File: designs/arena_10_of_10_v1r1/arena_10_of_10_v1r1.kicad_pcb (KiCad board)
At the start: 6 copper layers, 248.9 x 228.6 mm, 519 parts, among them J1 Cetus RJ45 Magjack, J10 Conn_01x05, J11 Conn_01x05, J12 Conn_01x05, J13 Conn_01x05, J14 Conn_01x05, J15 Conn_01x05, J16 Conn_01x05, J17 Conn_01x05, J18 Conn_01x05, J19 Conn_01x05, J2 Conn_01x02, J20 Conn_01x05, J21 Conn_01x05, J22 Conn_01x05, J23 Conn_01x05, J24 Conn_01x05, J25 Barrel_Jack, J26 Barrel_Jack, J27 Conn_Coaxial, J28 Conn_Coaxial, J29 Conn_Coaxial, J3 Conn_Coaxial, J4 Conn_Coaxial, J5 Conn_01x05, J6 Conn_01x05, J7 Conn_01x05, J8 Conn_01x05, J9 Conn_01x05, P1 NA, P10 NA, P2 NA, P3 NA, P4 NA, P5 NA, P6 NA, P7 NA, P8 NA, P9 NA, SW1 SW_SPDT, U1 Teensy4.1, U10 74LVC2G17, U100 74LVC1G125, U101 74LVC2G17, U102 SN74HCS08, U103 SN74HCS08, U104 74LVC1G125, U105 74LVC2G17, U106 SN74HCS08, U107 SN74HCS08, U108 74LVC1G125, U109 74LVC2G17, U11 74LVC2G17, U112 74LVC1G125, U113 74LVC2G17, U116 74LVC1G125, U117 74LVC2G17, U12 74LVC2G17, U120 74LVC1G125, U121 74LVC2G17, U124 74LVC1G125, U125 74LVC2G17, U13 74LVC2G17, U14 74LVC2G17, U15 74LVC2G17, U16 74LVC2G17, U17 74LVC2G17, U18 74LVC2G17, U19 74LVC2G17, U2 SN74LV1T34DBV, U20 74LVC2G17, U21 74LVC2G17, U22 74LVC2G17, U23 74LVC2G17, U24 74LVC2G17, U25 74LVC2G17, U26 74LVC2G17, U27 74LVC2G17, U28 74LVC2G17, U29 74LVC2G17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

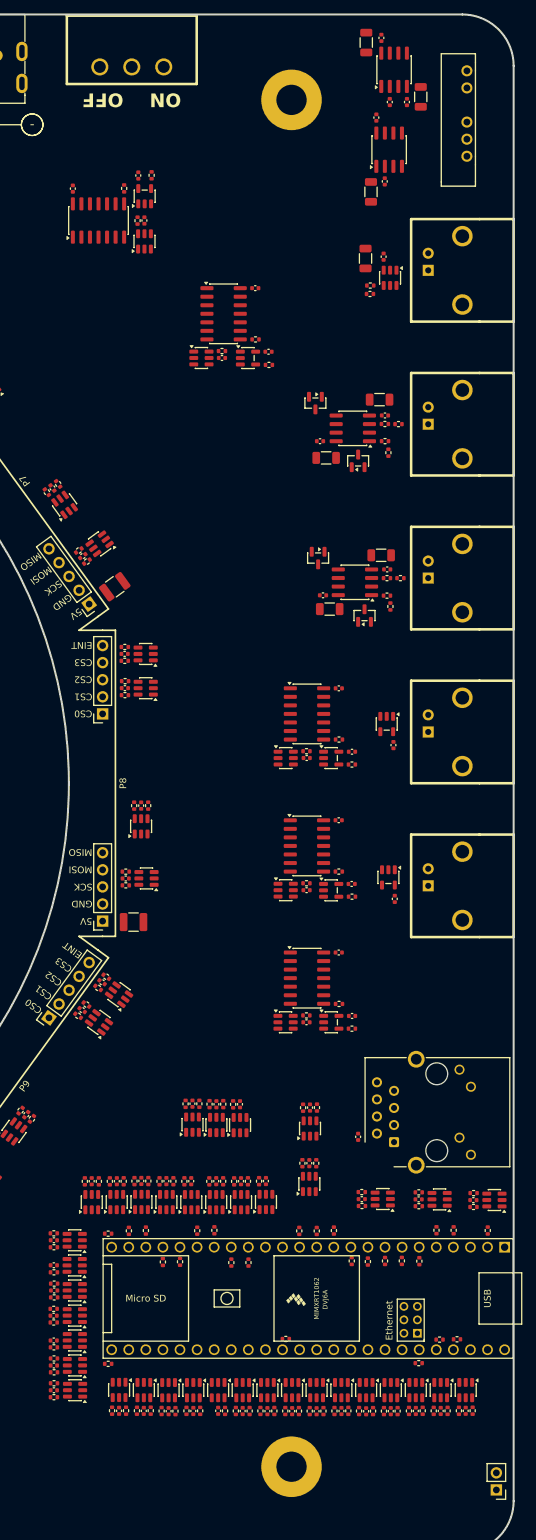
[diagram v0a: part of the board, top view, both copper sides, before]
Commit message: Added keepout zones, power plane fills, and routing boundry.
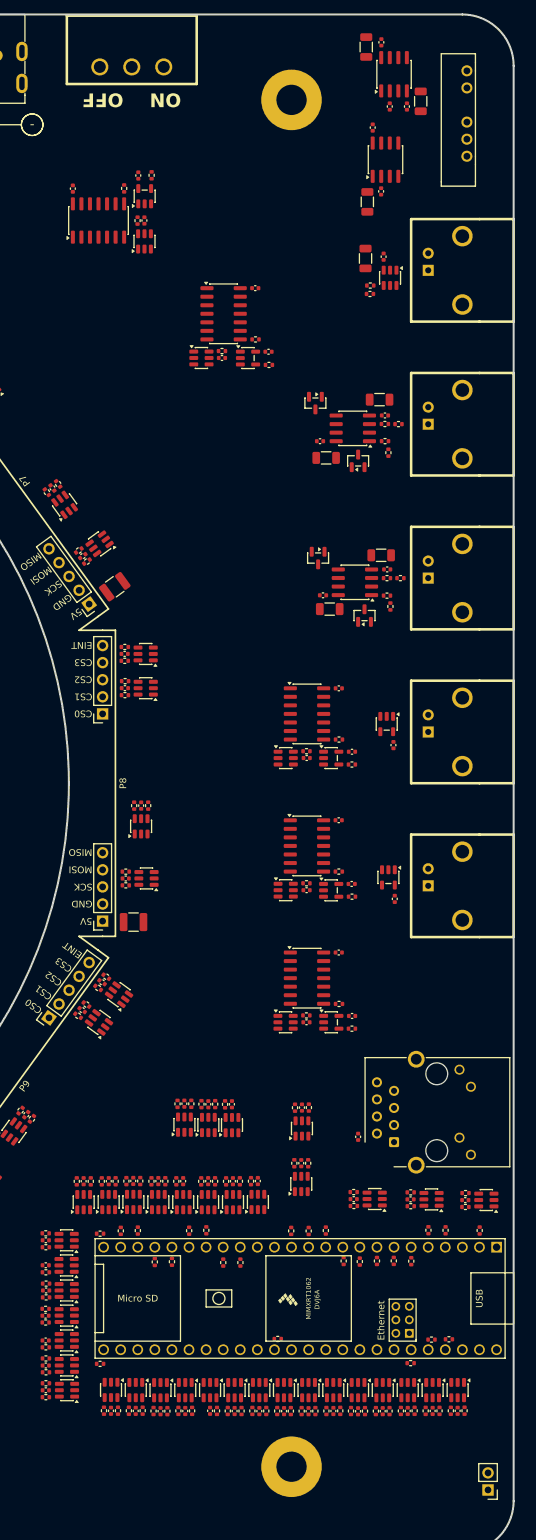
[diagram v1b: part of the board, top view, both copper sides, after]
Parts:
- moved U84 1.58 mm to (293.4, 85.1)
- moved C93 1.58 mm to (292.7, 89.8)
- moved C92 1.58 mm to (290.7, 91.4)
- moved C99 1.58 mm to (291.5, 80.3)
- moved J2 1.24 mm to (308.6, 282.9)
- moved C15 1.20 mm to (274.4, 236.9)
- moved C19 1.20 mm to (293.0, 271.1)
- moved C8 1.20 mm to (267.0, 225.5)
- moved R22 1.20 mm to (300.2, 260.5)
- moved R30 1.20 mm to (275.6, 271.1)
- moved R37 1.20 mm to (269.5, 225.5)
- moved R42 1.20 mm to (262.3, 237.0)
- moved R49 1.20 mm to (305.3, 238.7)
- moved R58 1.20 mm to (286.6, 271.1)
- moved R59 1.20 mm to (284.6, 271.1)
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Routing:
- added copper zone on In3.Cu, net +3.3V
- added copper zone on In2.Cu, net +5V
- added copper zone on In1.Cu, net GND
- added copper zone on In4.Cu, net GND
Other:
- board text added: "Remember to swap larger temporary diameter with smaller actual diameter after routing PCB"
